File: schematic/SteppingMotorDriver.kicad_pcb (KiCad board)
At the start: 2 copper layers, 100 x 100 mm, 110 parts, among them IC1 AM26LV32IDR, IC2 AM26LV32IDR, IC3 AM26LV32IDR, J1 5077CR-16SMC2-BK-TR, J10 Conn_01x04, J11 Conn_01x05, J12 Conn_01x04, J13 Conn_01x05, J2 Barrel_Jack_Switch, J3 Conn_01x02_Pin, J30 MOTOR_CH0, J31 MOTOR_CH1, J32 MOTOR_CH2, J4 Conn_01x04, J5 Conn_01x04_Pin, J6 Conn_01x04_Pin, J7 Conn_01x04_Pin, J8 Conn_01x02, J9 Conn_01x05, Q2 DMG3415, SW1 RESET, SW2 SW_Push, U1 NCP361SN, U2 ESP32-S3-WROOM-1, U3 MIC5219-3.3YM5, U5 LT6106, U6 NJM8532M, U7 NJM8532M, U8 NJM8532M

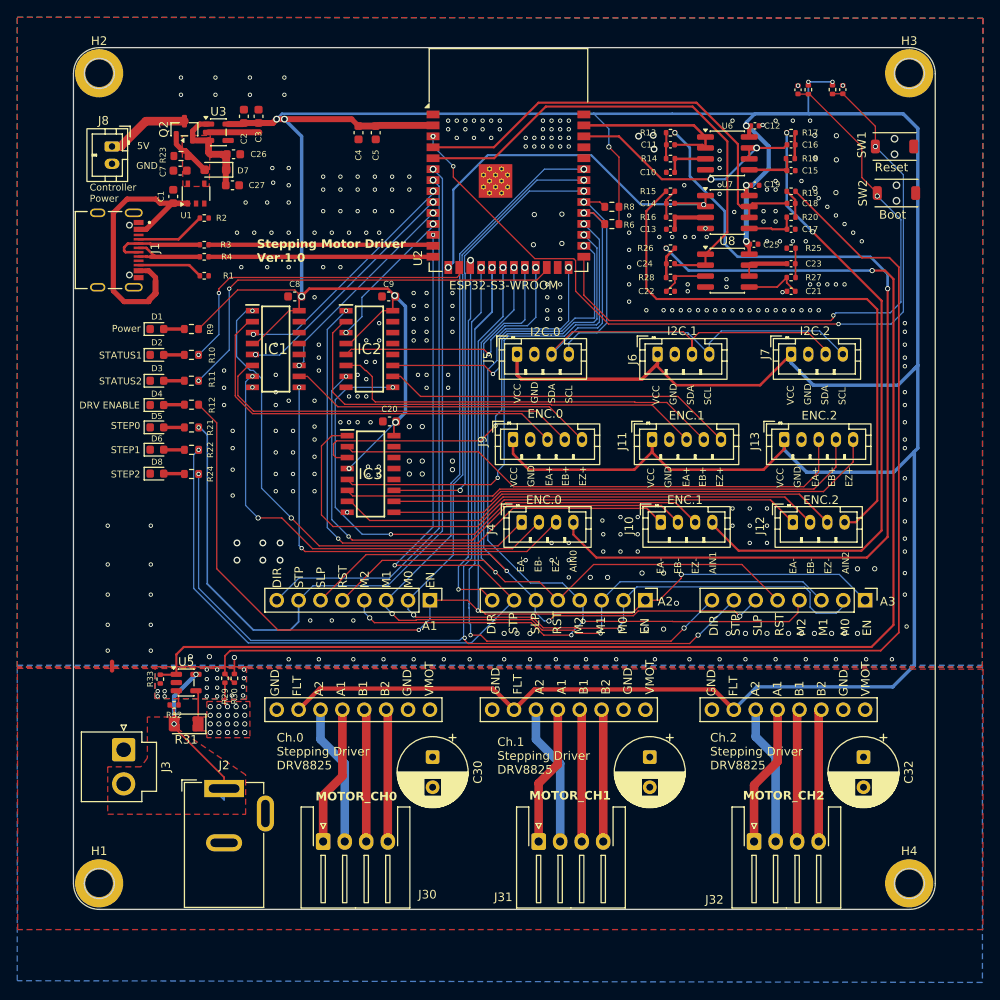
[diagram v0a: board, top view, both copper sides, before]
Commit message: Add status LED support, Multiplexer schematic, and Gerber export
Adds status_led.c/h for GPIO46/47 LED indicators, a Multiplexer
schematic sheet, exported Gerber fabrication files, and BLE Codex
prompt docs. Removes stale KiCad auto-backup zips.
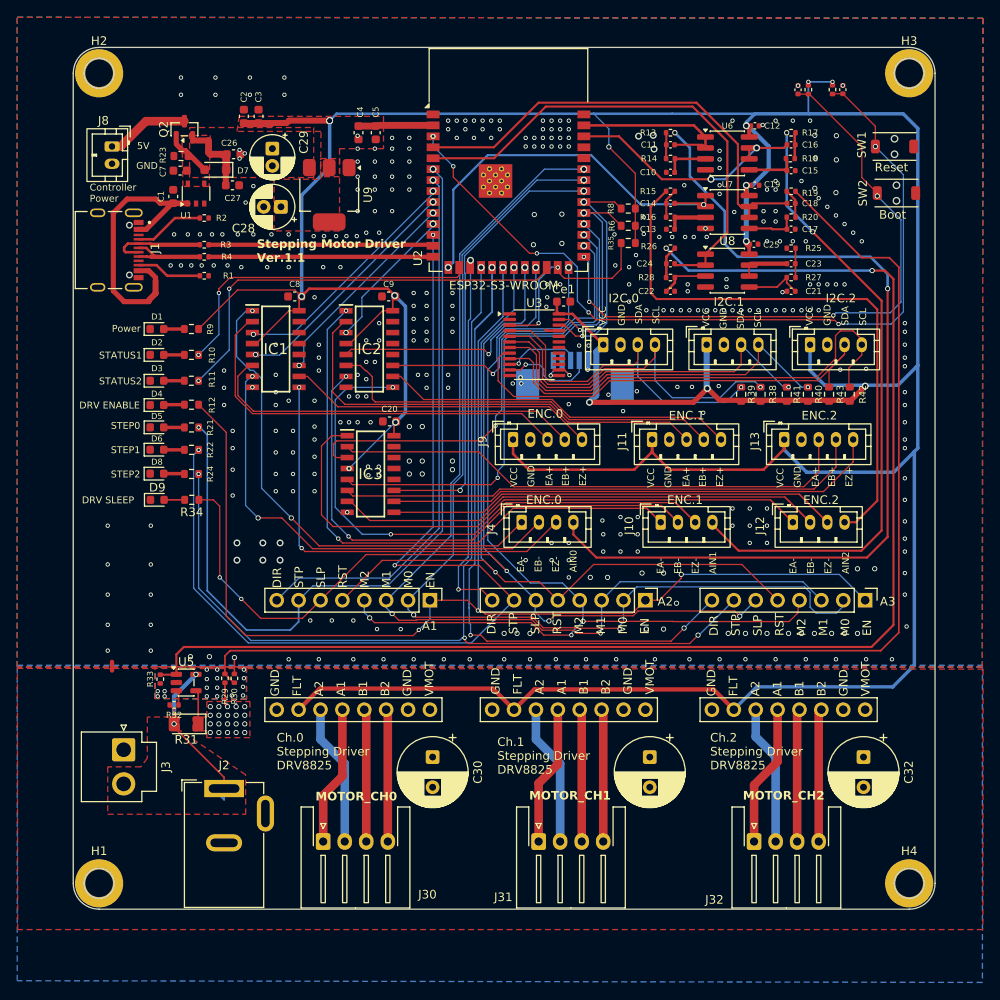
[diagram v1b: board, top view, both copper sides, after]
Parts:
- added C28: 100uf, Capacitor_THT:CP_Radial_D5.0mm_P2.00mm, F.Cu at (92.6, 62.0)
- added C29: 100uf, Capacitor_THT:CP_Radial_D5.0mm_P2.00mm, F.Cu at (91.6, 55.2)
- added Ce1: 0.1uF, Capacitor_SMD:C_0603_1608Metric, F.Cu at (125.4, 73.0)
- added D9: SLEEP LED, LED_SMD:LED_0603_1608Metric, F.Cu at (78.2, 96.0)
- added J15: Conn_01x06_MountingPin, Connector_FFC-FPC:TE_84953-6_1x06-1MP_P1.0mm_Horizontal, B.Cu at (126.7, 81.6)
- added R34: 1k, Resistor_SMD:R_0603_1608Metric, F.Cu at (82.2, 96.0)
- added R35: 10k, Resistor_SMD:R_0603_1608Metric, F.Cu at (132.9, 66.2)
- added R38: 2.2k, Resistor_SMD:R_0603_1608Metric, F.Cu at (148.2, 83.8)
- added R39: 2.2k, Resistor_SMD:R_0603_1608Metric, F.Cu at (146.0, 83.8)
- added R40: 2.2k, Resistor_SMD:R_0603_1608Metric, F.Cu at (153.8, 83.8)
- added R41: 2.2k, Resistor_SMD:R_0603_1608Metric, F.Cu at (151.3, 83.8)
- added R42: 2.2k, Resistor_SMD:R_0603_1608Metric, F.Cu at (158.6, 83.8)
- added R43: 2.2k, Resistor_SMD:R_0603_1608Metric, F.Cu at (156.2, 83.8)
- added U9: AMS1117-3.3, Package_TO_SOT_SMD:SOT-223-3_TabPin2, F.Cu at (98.2, 60.6)
- C27: value 1uF -> 0.1uF
- R32: value 499 -> 120
- R33: value 10k -> 5k
- U3: value MIC5219-3.3YM5 -> TCA9548APWR; footprint Package_TO_SOT_SMD:SOT-23-5 -> Package_SO:TSSOP-24_4.4x7.8mm_P0.65mm
- moved U3 44.2 mm to (122.0, 78.0)
- moved J5 10.1 mm to (130.0, 78.0)
- moved J6 5.81 mm to (142.0, 78.0)
- moved J7 2.46 mm to (154.0, 78.0)
- moved R6 1.91 mm to (132.9, 64.2)
- moved R8 1.91 mm to (132.9, 62.2)
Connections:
- J5 pad 3: I2C_SDA -> /I2C_Multiplexer/SDA0
- J5 pad 4: I2C_SCL -> /I2C_Multiplexer/SCL0
- J6 pad 3: I2C_SDA -> /I2C_Multiplexer/SDA1
- J6 pad 4: I2C_SCL -> /I2C_Multiplexer/SCL1
- J7 pad 3: I2C_SDA -> /I2C_Multiplexer/SDA2
- J7 pad 4: I2C_SCL -> /I2C_Multiplexer/SCL2
- U2 pad 25: unconnected-(U2-IO48-Pad25) -> I2C_MUL_RESET
- U3 pad 1: Net-(D7-K) -> GND
- U3 pad 3: Net-(D7-K) -> I2C_MUL_RESET
- U3 pad 4: unconnected-(U3-BP-Pad4) -> /I2C_Multiplexer/SDA0
- U3 pad 5: +3V3 -> /I2C_Multiplexer/SCL0
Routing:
- net /I2C_Multiplexer/SCL2: track 0.00 -> 55.0 mm
- net /I2C_Multiplexer/SDA2: track 0.00 -> 52.9 mm
- net /I2C_Multiplexer/SCL1: track 0.00 -> 43.9 mm, vias 0 -> 1
- net /I2C_Multiplexer/SCL0: track 0.00 -> 42.2 mm, vias 0 -> 1
- net /I2C_Multiplexer/SDA1: track 0.00 -> 41.9 mm, vias 0 -> 1
- net /I2C_Multiplexer/SDA0: track 0.00 -> 40.0 mm, vias 0 -> 1
- net I2C_SDA: track 62.3 -> 25.2 mm, vias 1 -> 2
- net I2C_SCL: track 59.3 -> 26.7 mm, vias 1 -> 2
- net DRV_SLEEP: track 97.7 -> 123.2 mm, vias 4 -> 6
- net I2C_MUL_RESET: track 0.00 -> 22.7 mm, vias 0 -> 2
- net +3V3: track 486.9 -> 501.5 mm, vias 12 -> 15
- net Net-(J15-Pin_3): track 0.00 -> 12.0 mm, vias 0 -> 1
- net Net-(J15-Pin_4): track 0.00 -> 9.01 mm, vias 0 -> 1
- net GND: track 8.57 -> 3.51 mm, vias 357 -> 389
- net Net-(J15-Pin_5): track 0.00 -> 3.60 mm, vias 0 -> 1
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- added copper zone on F.Cu, net +3V3
- added copper zone on F.Cu, net Net-(D7-K)
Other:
- board text added: "DRV SLEEP"
- board text added: "Stepping Motor Driver Ver.1.1"
- board text removed: "Stepping Motor Driver Ver.1.0"
